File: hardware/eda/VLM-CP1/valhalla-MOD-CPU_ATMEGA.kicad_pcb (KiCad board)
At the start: 2 copper layers, 76.2 x 50.8 mm, 35 parts, among them J1 GPIO, J3 BUS, K1 RESET, U1 ATmega328P-P, U2 74LS06, U3 74LS07, U4 L78L33_TO92, Y1 7.3728 MHz

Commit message: UPDATE: PSU and CPU(ATMega-T) artwork complete
 - also extracted the existing PSU as a template for future modules
 - PSU final touches and RTM
 - CPU(ATMega-T) tied unused inputs to GND, fixed all DRC violations,
   dressed-up silkscreen and RTM.
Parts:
- moved C1 7.47 mm to (99.6, 76.7), turned to -90 degrees
- moved C3 1.88 mm to (105.4, 76.7), turned to -90 degrees
- renumbered J3 to J1, J1 to J2
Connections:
- U2 pad 10: (no net) -> unconnected-(U2-Pad10)
- U2 pad 11: (no net) -> /DGND
- U2 pad 12: (no net) -> unconnected-(U2-Pad12)
- U2 pad 13: (no net) -> /DGND
- U2 pad 5: (no net) -> /DGND
- U2 pad 6: (no net) -> unconnected-(U2-Pad6)
- U2 pad 8: (no net) -> unconnected-(U2-Pad8)
- U2 pad 9: (no net) -> /DGND
- U3 pad 10: (no net) -> unconnected-(U3-Pad10)
- U3 pad 11: (no net) -> /DGND
- U3 pad 12: (no net) -> unconnected-(U3-Pad12)
- U3 pad 13: (no net) -> /DGND
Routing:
- net /DVCC: track 16.0 -> 0.00 mm, vias 4 -> 0
- net Net-(D2-K): track 28.3 -> 35.2 mm, vias 0 -> 2
- net Net-(D1-K): track 28.3 -> 30.9 mm, vias 0 -> 1
- net /SDA: track 19.4 -> 17.6 mm, vias 2 -> 1
- net /SCK: track 67.3 -> 65.7 mm
- net /GPIO7: track 51.1 -> 49.6 mm
- net Net-(D2-A): track 8.93 -> 10.3 mm
- net /~{RTS}: track 74.1 -> 75.4 mm
- net /~{IINT}: track 58.9 -> 58.0 mm
- net /GPIO5: track 37.1 -> 38.0 mm, vias 1 -> 2
- net /SCL: track 52.6 -> 51.8 mm
- net Net-(JP1-B): track 11.4 -> 10.7 mm
- net Net-(D5-A): track 8.10 -> 7.45 mm
- net Net-(D6-K): track 17.2 -> 16.7 mm
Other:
- board text added: "20250126"
- board text added: "BOTC"
- board text added: "BUS"
- board text added: "CPU(ATMega-T)"
- board text added: "GPIO"
- board text added: "RESET"
- board text added: "TOPC"
- board text added: "TOPS"
- board text added: "Valhalla-MOD"

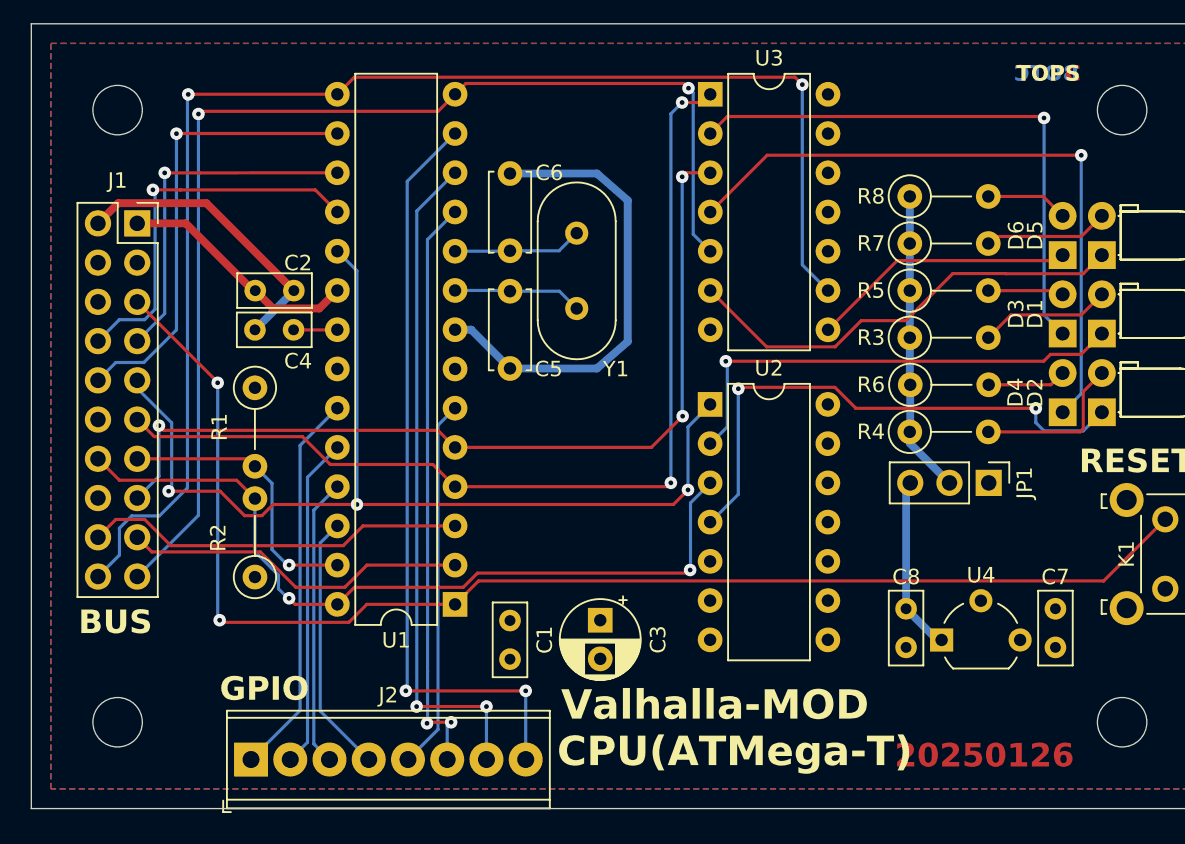
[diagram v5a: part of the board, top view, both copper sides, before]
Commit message: UPDATE: updated MOD-CPU(ATMega) to match the latest specification.
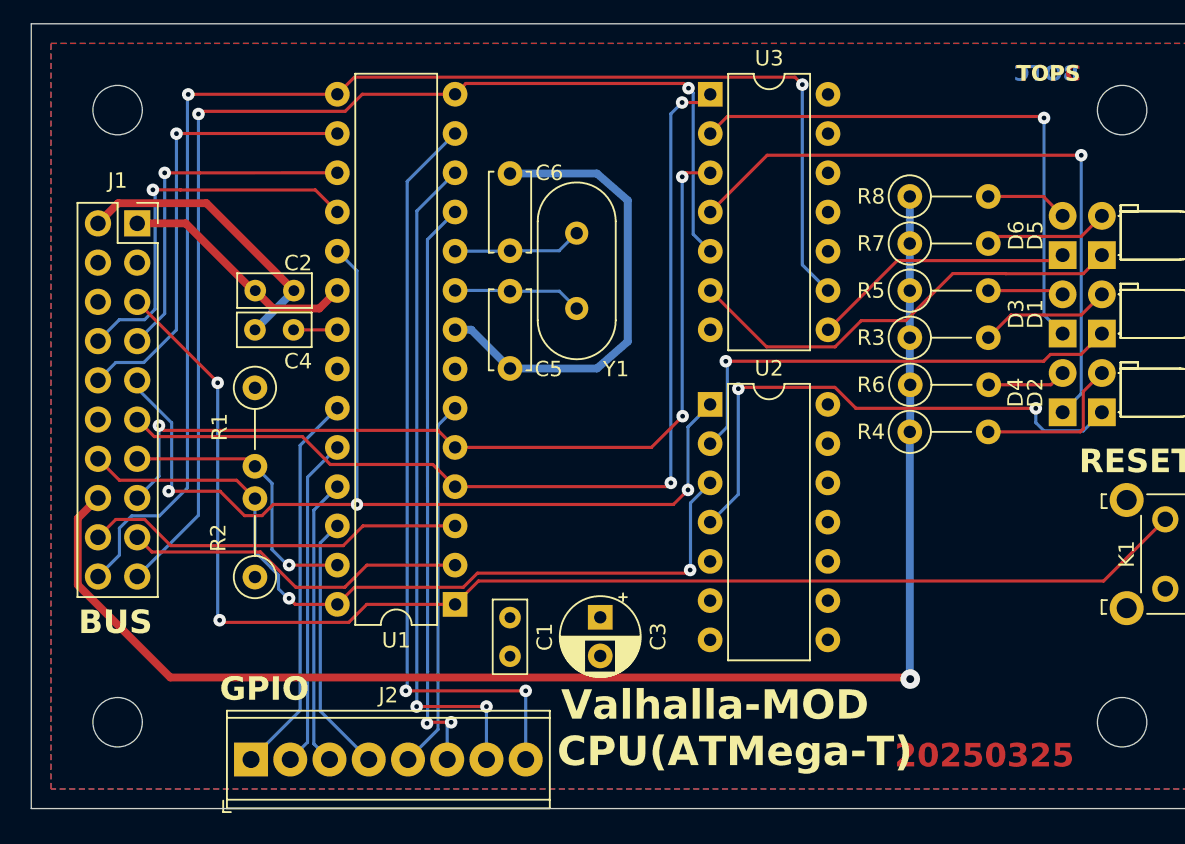
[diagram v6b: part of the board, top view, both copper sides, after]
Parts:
- removed C7: 330nF, Capacitor_THT:C_Rect_L4.6mm_W2.0mm_P2.50mm_MKS02_FKP02
- removed C8: 0.1uF, Capacitor_THT:C_Rect_L4.6mm_W2.0mm_P2.50mm_MKS02_FKP02
- removed JP1: LED_VCC, Connector_PinHeader_2.54mm:PinHeader_1x03_P2.54mm_Vertical
- removed U4: L78L33_TO92, Package_TO_SOT_THT:TO-92_Wide
- D1, D2, D3, D4, D5, D6: value *2 -> R
- R3, R4, R5, R6, R7, R8: value *1 -> 1K
- moved C1 0.19 mm to (99.6, 76.5)
- moved C3 0.19 mm to (105.4, 76.5)
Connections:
- J1 pad 16: unconnected-(J1-Pin_16-Pad16) -> /LVCC
- J1 pad 6: unconnected-(J1-Pin_6-Pad6) -> /DGND
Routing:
- net /LVCC: track 19.5 -> 93.8 mm, vias 0 -> 1
- net Net-(JP1-B): track 10.7 -> 0.00 mm
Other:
- board text added: "20250325"
- board text removed: "20250126"
